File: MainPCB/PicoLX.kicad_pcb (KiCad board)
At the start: 2 copper layers, 129.5 x 70.6 mm, 84 parts, among them J1 USB_C_Receptacle_USB2.0, SW1 SW_Push, SW2 Test, SW3 Service, U1 RP2040, U2 W25Q32JVSS, U3 NCP1117-3.3_SOT223, U4 SN74LV1T34DBV, Y1 12.000MHz

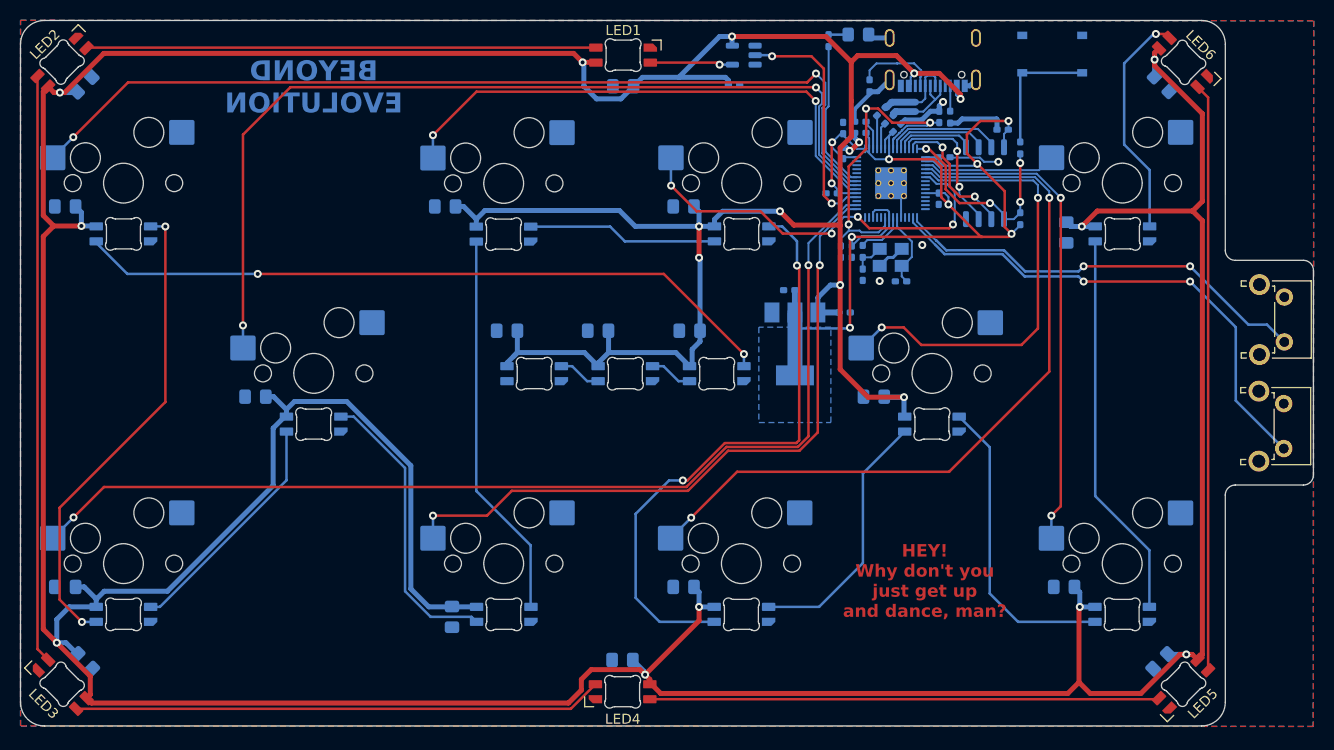
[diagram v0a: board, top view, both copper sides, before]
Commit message: Fixed minor switch alignment issues (<0.05mm)
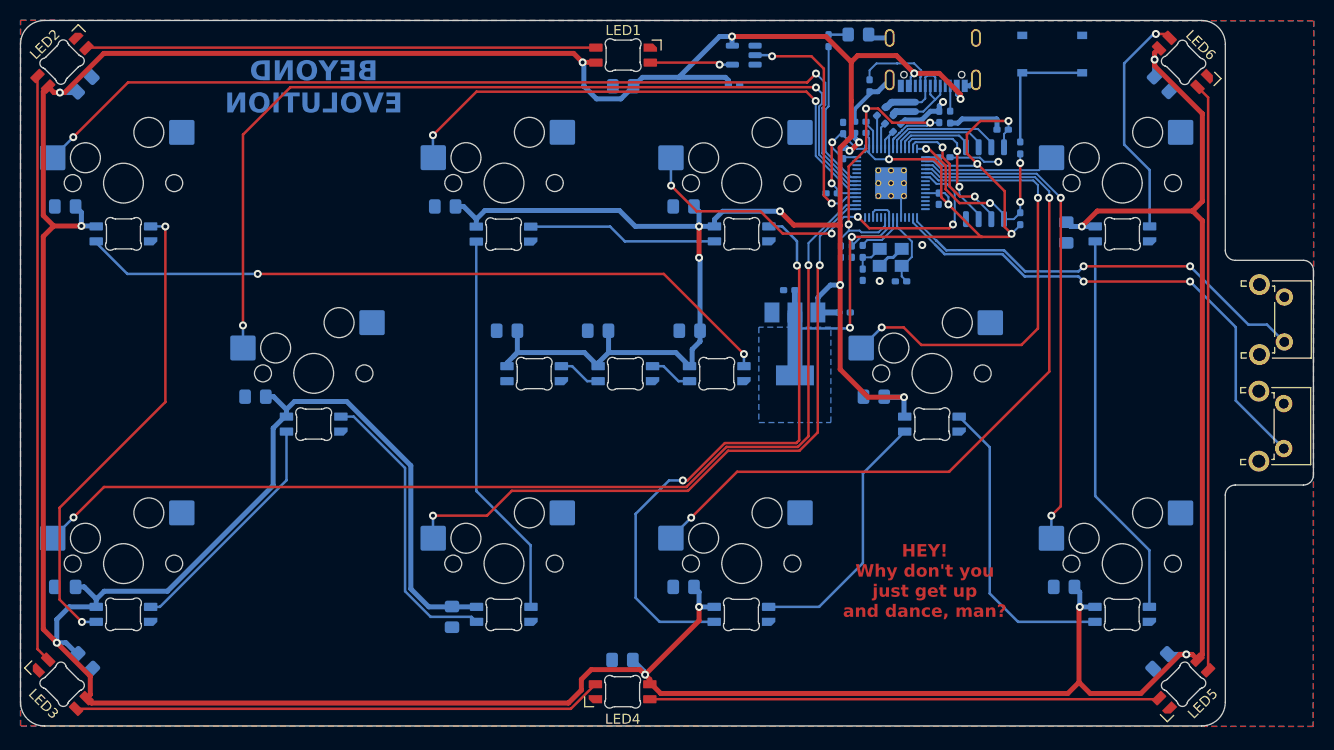
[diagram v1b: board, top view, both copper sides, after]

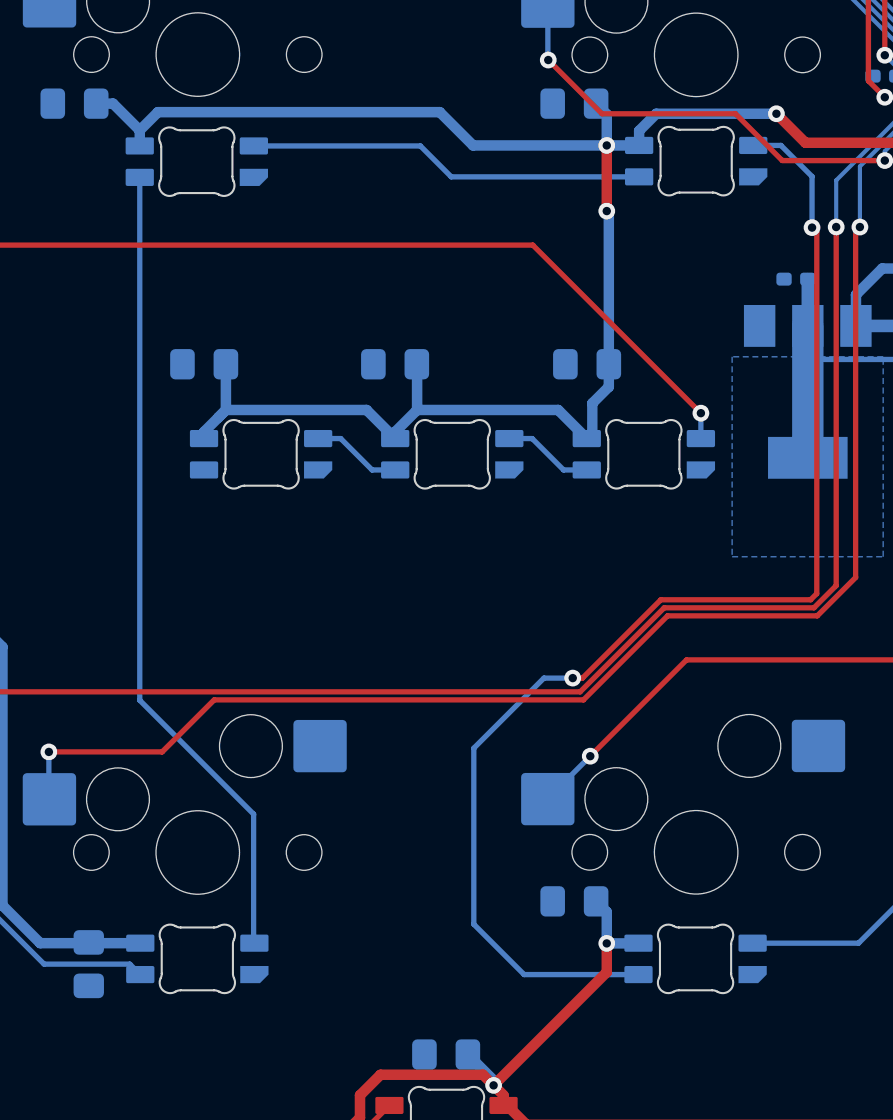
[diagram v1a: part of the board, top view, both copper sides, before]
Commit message: Update README, several minor adjustments
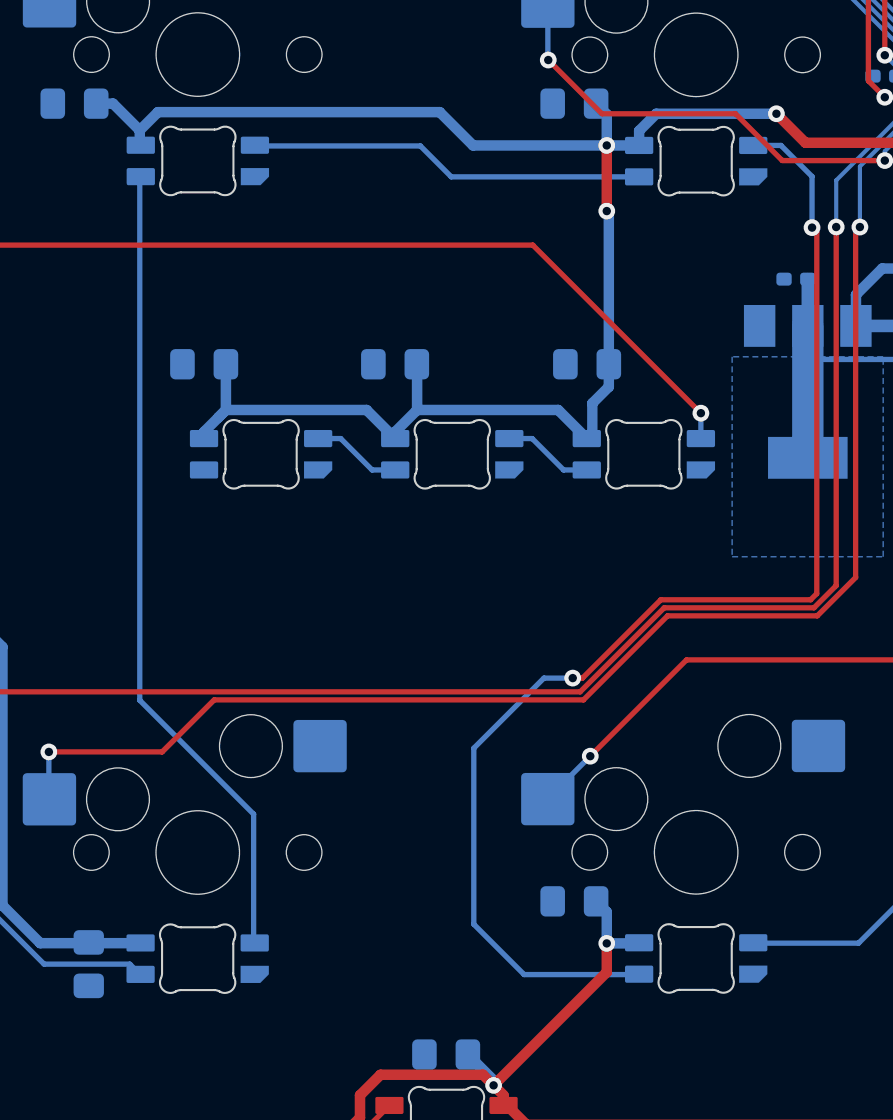
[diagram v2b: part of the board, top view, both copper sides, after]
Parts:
- moved LED12 0.06 mm to (147.4, 82.3)
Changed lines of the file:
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@@
   )
   (footprint "marbastlib-various:LED_6028R" (layer "B.Cu")
-    (at 171.22 120.45 180)
+    (at 171.25 120.430001 180)
     (descr "rear-mount SMD 6028 RGB LED")
     (tags "LED RGB 6028 rear mount reverse")
@@
   )
   (footprint "marbastlib-various:LED_6028R" (layer "B.Cu")
-    (at 147.4 82.375 180)
+    (at 147.45 82.34 180)
     (descr "rear-mount SMD 6028 RGB LED")
     (tags "LED RGB 6028 rear mount reverse")
@@
   )
   (footprint "marbastlib-various:LED_6028R" (layer "B.Cu")
-    (at 147.425 120.45 180)
+    (at 147.44 120.44 180)
     (descr "rear-mount SMD 6028 RGB LED")
     (tags "LED RGB 6028 rear mount reverse")
